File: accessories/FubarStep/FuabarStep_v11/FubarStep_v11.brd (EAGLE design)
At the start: 100.3 x 49.5 mm, 59 parts, among them IC2 SN754410NE, IC3 SN754410NE, U1 FUBARINO_SD, U2 FUBARINO_MINI, U3 OKI-78SR-5/1.5-W36H-C, X1 DC21MMX

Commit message: Fixed a minor silk screen error from FubarStep v1.0 Added RoSH and CE logos to back silk
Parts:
- added U$2: (no value), SchmalzHausPublic:ROHS_GARBAGE_5MM
- added U$3: (no value), SchmalzHausPublic:CE_5MM
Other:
- board text added: "+3V3"
- board text added: "FUBARStep v1.1 Creatded by FUBARLabs and Schmalz Haus www.fubarlabs.org www.schmalzhaus.com www.fubarino.org"
- board text removed: "FUBARStep v1.0 Creatded by FUBARLabs and Schmalz Haus www.fubarlabs.org www.schmalzhaus.com www.fubarino.org"
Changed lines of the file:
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@@
 <grid distance="0.05" unitdist="inch" unit="inch" style="lines" multiple="1" display="yes" altdistance="5" altunitdist="mil" altunit="inch"/>
 <layers>
-<layer number="1" name="Top" color="4" fill="1" visible="yes" active="yes"/>
-<layer number="16" name="Bottom" color="1" fill="1" visible="yes" active="yes"/>
+<layer number="1" name="Top" color="4" fill="1" visible="no" active="yes"/>
+<layer number="16" name="Bottom" color="1" fill="1" visible="no" active="yes"/>
 <layer number="17" name="Pads" color="2" fill="1" visible="yes" active="yes"/>
 <layer number="18" name="Vias" color="14" fill="1" visible="yes" active="yes"/>
-<layer number="19" name="Unrouted" color="6" fill="1" visible="yes" active="yes"/>
-<layer number="20" name="Dimension" color="15" fill="1" visible="yes" active="yes"/>
-<layer number="21" name="tPlace" color="7" fill="1" visible="yes" active="yes"/>
-<layer number="22" name="bPlace" color="7" fill="1" visible="no" active="yes"/>
-<layer number="23" name="tOrigins" color="15" fill="1" visible="yes" active="yes"/>
-<layer number="24" name="bOrigins" color="15" fill="1" visible="no" active="yes"/>
+<layer number="19" name="Unrouted" color="6" fill="1" visible="no" active="yes"/>
+<layer number="20" name="Dimension" color="15" fill="1" visible="no" active="yes"/>
+<layer number="21" name="tPlace" color="7" fill="1" visible="no" active="yes"/>
+<layer number="22" name="bPlace" color="7" fill="1" visible="yes" active="yes"/>
+<layer number="23" name="tOrigins" color="15" fill="1" visible="no" active="yes"/>
+<layer number="24" name="bOrigins" color="15" fill="1" visible="yes" active="yes"/>
 <layer number="25" name="tNames" color="7" fill="1" visible="no" active="yes"/>
 <layer number="26" name="bNames" color="7" fill="1" visible="no" active="yes"/>
@@
 <text x="44.958" y="44.704" size="1.016" layer="21" font="vector" ratio="10" rot="R90">TX-&gt;</text>
 <text x="47.371" y="44.704" size="1.016" layer="21" font="vector" ratio="10" rot="R90">RX&lt;-</text>
-<text x="7.112" y="45.212" size="1.016" layer="21" font="vector" ratio="10">+5V</text>
+<text x="6.223" y="45.212" size="1.016" layer="21" font="vector" ratio="10">+3V3</text>
 <text x="7.112" y="47.752" size="1.016" layer="21" font="vector" ratio="10">GND</text>
 <text x="41.021" y="12.954" size="2.032" layer="21" font="vector" ratio="15">FUBARStep v1.1</text>
@@
 <text x="8.001" y="42.545" size="1.016" layer="21" font="vector" ratio="10">A0</text>
 <text x="64.135" y="42.672" size="1.016" layer="21" font="vector" ratio="10">A14</text>
-<text x="65.278" y="19.177" size="1.778" layer="22" font="vector" ratio="10" rot="MR0">FUBARStep v1.0
+<text x="65.278" y="19.177" size="1.778" layer="22" font="vector" ratio="10" rot="MR0">FUBARStep v1.1
 Creatded by FUBARLabs and Schmalz Haus
 www.fubarlabs.org
@@
 <text x="72.39" y="1.143" size="1.016" layer="21" font="vector" ratio="10">GND</text>
 <text x="86.36" y="1.143" size="1.016" layer="21" font="vector" ratio="10">GND</text>
-<text x="91.059" y="20.828" size="1.016" layer="21" font="vector" ratio="10">M1</text>
-<text x="90.932" y="9.906" size="1.016" layer="21" font="vector" ratio="10">M2</text>
-<text x="90.297" y="16.002" size="1.016" layer="21" font="vector" ratio="10">GND</text>
-<text x="91.059" y="39.751" size="1.016" layer="21" font="vector" ratio="10">M1</text>
-<text x="90.17" y="33.909" size="1.016" layer="21" font="vector" ratio="10">GND</text>
-<text x="90.932" y="28.575" size="1.016" layer="21" font="vector" ratio="10">M2</text>
+<text x="92.202" y="20.701" size="1.016" layer="21" font="vector" ratio="10" rot="R90">M1</text>
+<text x="92.075" y="9.779" size="1.016" layer="21" font="vector" ratio="10" rot="R90">M2</text>
+<text x="92.075" y="14.478" size="1.016" layer="21" font="vector" ratio="10" rot="R90">GND</text>
+<text x="92.075" y="39.37" size="1.016" layer="21" font="vector" ratio="10" rot="R90">M1</text>
+<text x="92.202" y="33.02" size="1.016" layer="21" font="vector" ratio="10" rot="R90">GND</text>
+<text x="92.202" y="26.416" size="1.016" layer="21" font="vector" ratio="10" rot="R90">M2</text>
 </plain>
 <attributes>
@@
 <element name="JP37" library="SparkFun-Connectors" package="SCREWTERMINAL-3.5MM-2" value="" x="96.52" y="19.558" rot="R90"/>
 <element name="JP38" library="SparkFun-Connectors" package="SCREWTERMINAL-3.5MM-3" value="" x="96.52" y="8.509" rot="R90"/>
+<element name="U$2" library="SchmalzHausPublic" package="ROHS_GARBAGE_5MM" value="" x="21.463" y="22.987" rot="MR0"/>
+<element name="U$3" library="SchmalzHausPublic" package="CE_5MM" value="" x="27.559" y="25.527" rot="MR0"/>
 </elements>
 <signals>

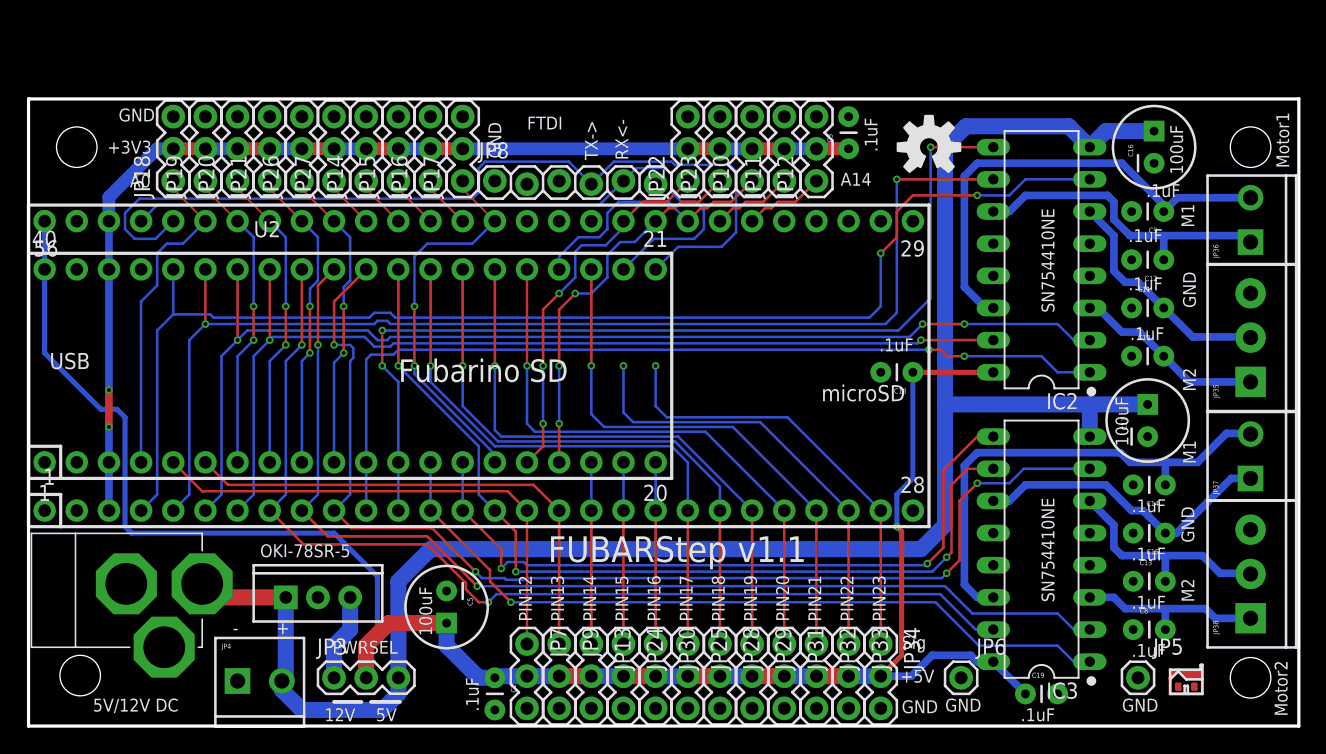
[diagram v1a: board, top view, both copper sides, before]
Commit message: Made board taller so that we could fit screws into the mounding holes. Added silk on all pins for better documentation. Ordered this exact board from OSHPark.
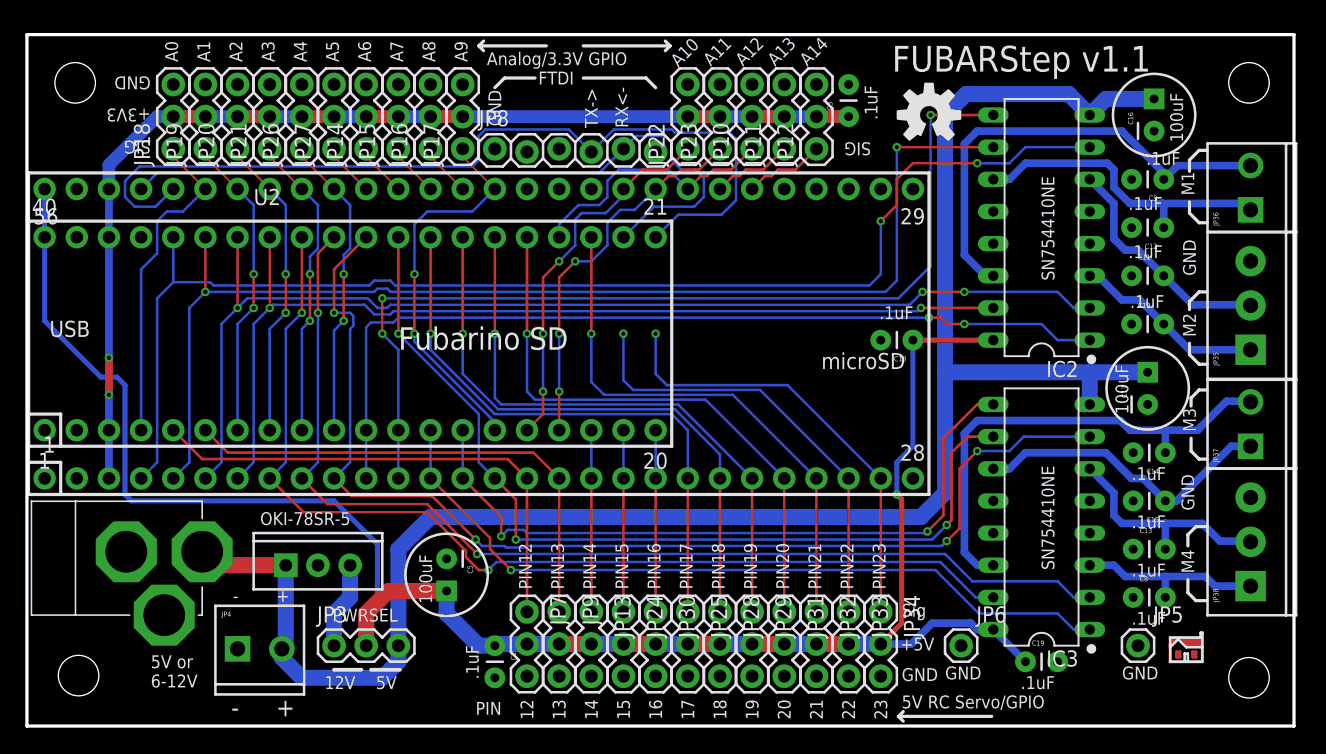
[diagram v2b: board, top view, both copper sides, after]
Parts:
- moved JP10 2.54 mm to (57.1, 45.6)
- moved JP11 2.54 mm to (59.7, 45.6)
- moved JP12 2.54 mm to (62.2, 45.6)
- moved JP14 2.54 mm to (26.7, 45.6)
- moved JP15 2.54 mm to (29.2, 45.6)
- moved JP16 2.54 mm to (31.8, 45.6)
- moved JP17 2.54 mm to (34.3, 45.6)
- moved JP18 2.54 mm to (11.4, 45.6)
- moved JP19 2.54 mm to (14.0, 45.6)
- moved JP20 2.54 mm to (16.5, 45.6)
- moved JP21 2.54 mm to (19.1, 45.6)
- moved JP22 2.54 mm to (52.1, 45.6)
- moved JP23 2.54 mm to (54.6, 45.6)
- moved JP26 2.54 mm to (21.6, 45.6)
- moved JP27 2.54 mm to (24.1, 45.6)
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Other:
- board size 100.3 x 49.5 mm -> 100.1 x 54.6 mm
- board text added: "12"
- board text added: "13"
- board text added: "14"
- board text added: "15"
- board text added: "16"
- board text added: "17"
- board text added: "18"
- board text added: "19"
- board text added: "20"
- board text added: "21"
- board text added: "22"
- board text added: "23"
- board text added: "5V RC Servo/GPIO"
- board text added: "5V or 6-12V"
- board text added: "A1"
- board text added: "A10"
- board text added: "A11"
- board text added: "A12"
- board text added: "A13"
- board text added: "A2"
- board text added: "A3"
- board text added: "A4"
- board text added: "A5"
- board text added: "A6"
- board text added: "A7"
- board text added: "A8"
- board text added: "A9"
- board text added: "Analog/3.3V GPIO"
- board text added: "M3"
- board text added: "M4"
- board text added: "PIN"
- board text added: "SIG"
- board text removed: "5V/12V DC"
- board text removed: "Motor1"
- board text removed: "Motor2"
